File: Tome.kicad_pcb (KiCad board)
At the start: 2 copper layers, 13 x 1.4 mm, 155 parts, among them J201 USB_C_Receptacle_USB2.0_14P, J202 SD_Card_Receptacle, J203 [battery], J204 FFC Connector, J205 SM03B-SRSS-TB, J301 FFC Connector, J302 AudioJack3, J401 FPC Connector, J501 FPC Connector, J601 Conn_01x02_Pin, J602 Conn_01x02_Pin, J603 Conn_01x02_Pin, J604 Conn_01x02_Pin, J701 Conn_01x02_Pin, J702 Conn_01x02_Pin, J703 Conn_01x02_Pin, J704 Conn_01x02_Pin, Q201 DMG3415, Q202 DMG3415, Q401 Si1308EDL, Q501 Si1308EDL, SW201 [bootstrap button], SW202 [reset button], SW203 SW_SPST, SW301 SW_SPST, SW302 SW_SPST, SW601 RotaryEncoder_Switch, SW701 RotaryEncoder_Switch, U201 MCP73831-2-OT, U202 XC6220B331MR, U203 W25Q128JVS, U204 RP2350A, U205 74AHC1G04, U206 W25Q128JVS, U301 TLV70033_SOT23-5, U302 PCM5102A, U303 PAM8908, Y201 ABM8-272-T3

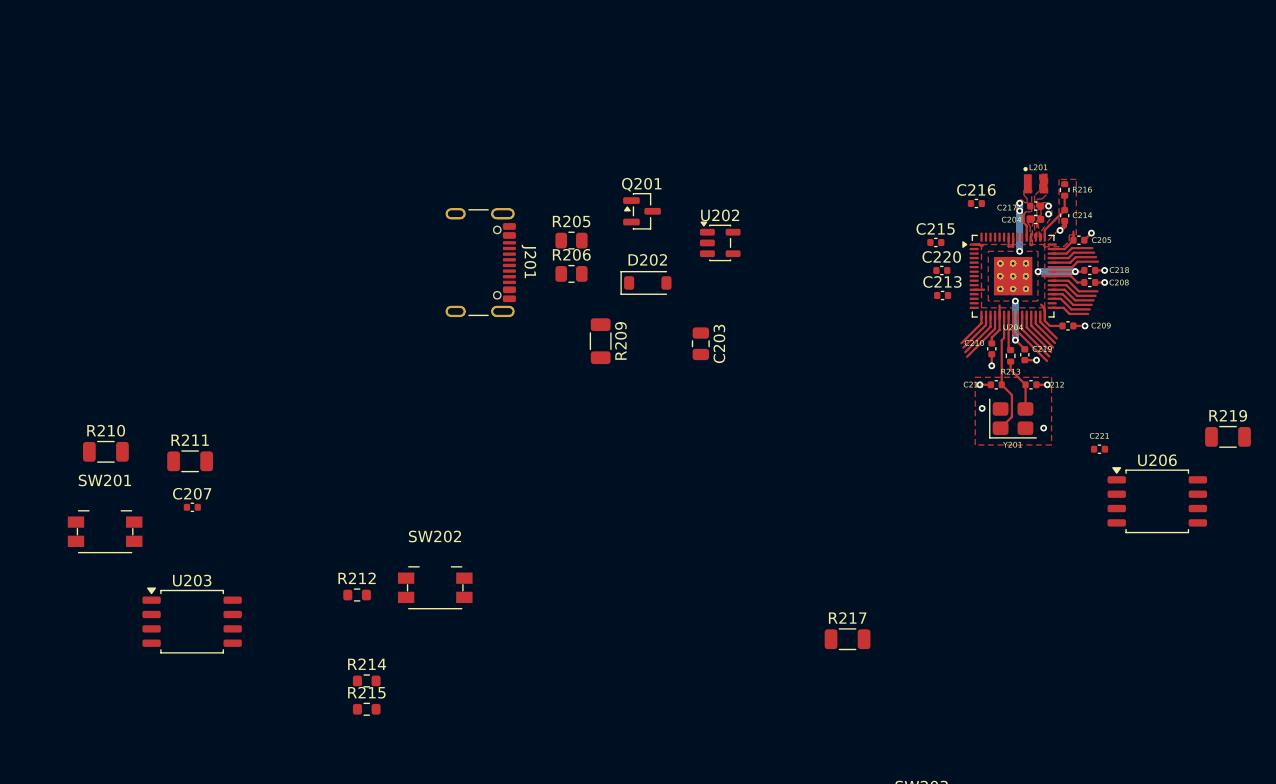
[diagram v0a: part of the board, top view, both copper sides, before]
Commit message: flash chip and usb data lines
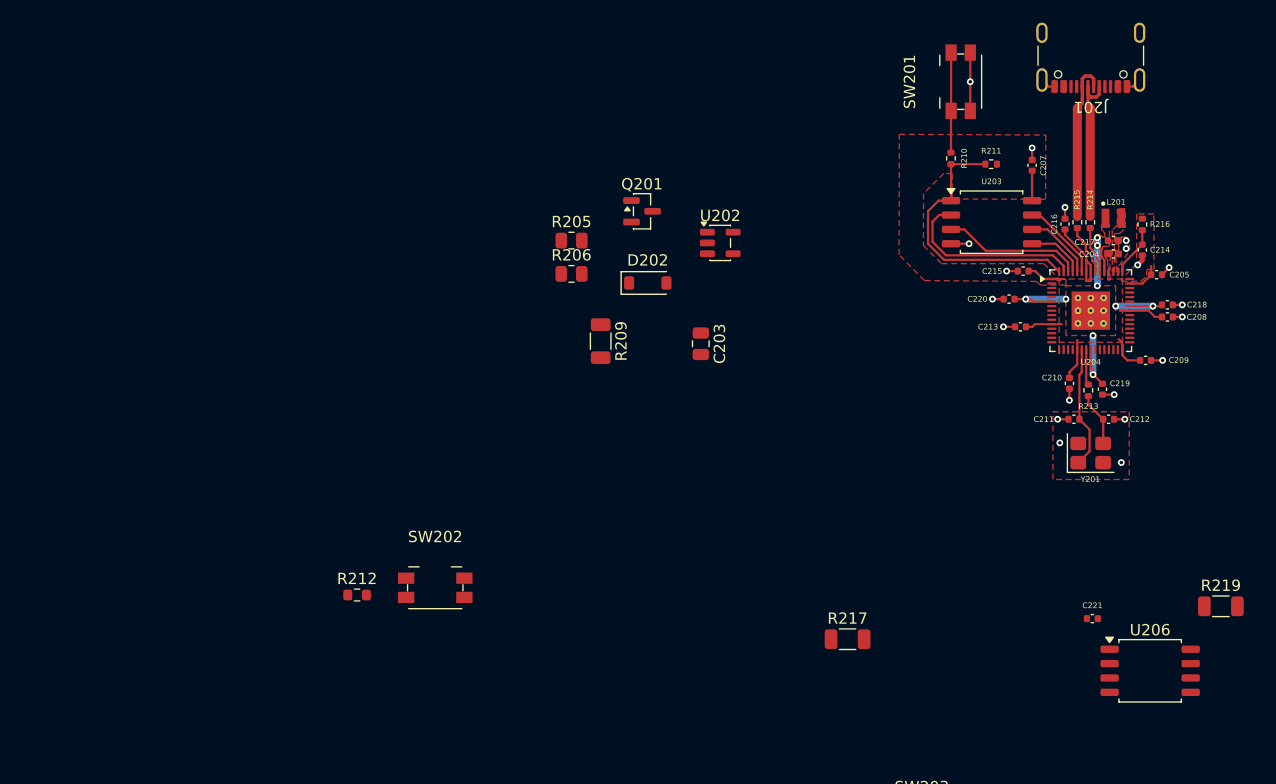
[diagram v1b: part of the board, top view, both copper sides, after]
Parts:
- R210, R211: footprint Resistor_SMD:R_1206_3216Metric -> Resistor_SMD:R_0402_1005Metric
- R214, R215: footprint Resistor_SMD:R_0603_1608Metric -> Resistor_SMD:R_0402_1005Metric
- moved SW201 85.5 mm to (256.4, 23.3), turned to 90 degrees
- moved C207 80.2 mm to (262.7, 30.7), turned to -90 degrees
- moved R210 79.1 mm to (255.5, 30.1), turned to -90 degrees
- moved U203 79.1 mm to (259.1, 35.8)
- moved R215 76.2 mm to (266.7, 35.8), turned to -90 degrees
- moved R214 75.8 mm to (267.9, 35.8), turned to -90 degrees
- moved R211 75.6 mm to (259.1, 30.6)
- moved J201 58.4 mm to (267.9, 20.1), turned to 180 degrees
- moved R219 15.0 mm to (279.4, 69.8)
- moved U206 15.0 mm to (273.2, 75.5)
- moved C221 15.0 mm to (268.1, 70.8)
- moved C215 8.13 mm to (261.9, 40.1), turned to 180 degrees
- moved C216 8.05 mm to (265.6, 35.9), turned to 90 degrees
- moved C205 7.52 mm to (273.7, 40.4)
- moved C210 7.52 mm to (266.0, 50.0)
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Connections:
- J201 pad SH: (no net) -> GND
- R214 pad 1: USB_D+ -> USB_D-
- R215 pad 1: USB_D- -> USB_D+
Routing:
- net FLASH_CS_1: track 0.00 -> 24.2 mm
- net QSPI_D1: track 0.00 -> 16.7 mm
- net GND: track 8.59 -> 23.1 mm, vias 13 -> 20
- net USB_D-: track 0.00 -> 14.2 mm
- net USB_D+: track 0.00 -> 14.2 mm
- net +3V3: track 17.6 -> 30.7 mm
- net QSPI_D2: track 0.00 -> 12.4 mm
- net Net-(R210-Pad1): track 0.00 -> 8.85 mm
- net QSPI_D3: track 0.00 -> 7.22 mm
- net +1V1: track 19.5 -> 26.4 mm, vias 7 -> 9
- net QSPI_SCLK: track 0.00 -> 6.19 mm
- net QSPI_D0: track 0.00 -> 5.17 mm
- net Net-(J205-Pin_1): track 5.14 -> 0.00 mm
- net DISPLAY_RESET_L: track 4.71 -> 0.00 mm
- net Net-(J205-Pin_3): track 4.66 -> 0.00 mm
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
